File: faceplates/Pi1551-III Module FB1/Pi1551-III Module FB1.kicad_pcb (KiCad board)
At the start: 2 copper layers, 100 x 100 mm, 8 parts, among them M1 Mounting, M2 Mounting, M3 Mounting, M4 Mounting

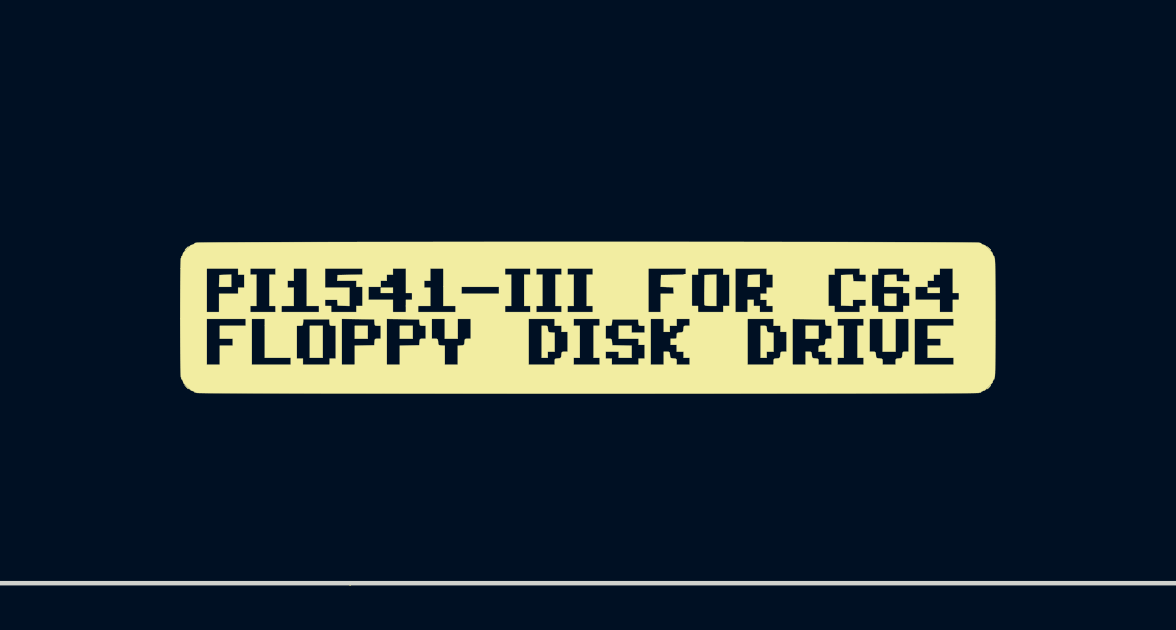
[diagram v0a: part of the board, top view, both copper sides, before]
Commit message: PI1551 branding and Microgramma font labels
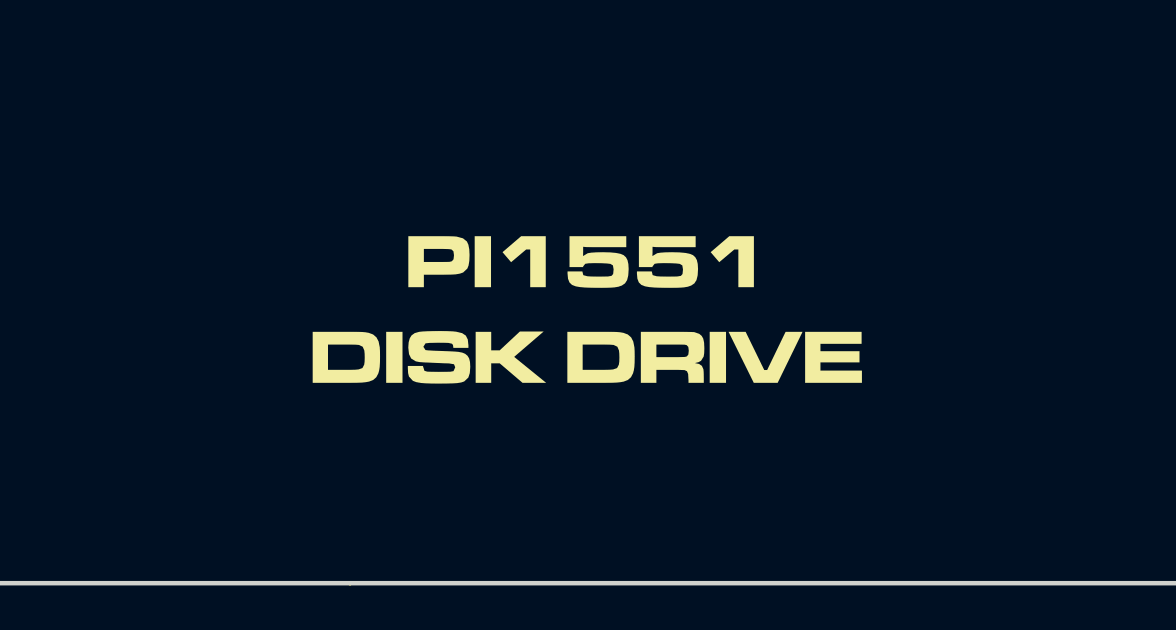
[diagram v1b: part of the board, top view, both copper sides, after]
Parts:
- removed G***: LOGO, Pi1541:Pi1541-Decal2
- removed Pi1541-logo3: , Pi1541:Pi1541-logo3
- added kibuzzard-69864CDD: G***, kibuzzard-69864CDD, B.Cu at (120.2, 91.0)
- added kibuzzard-69864D02: G***, kibuzzard-69864D02, B.Cu at (120.2, 83.0)
- added kibuzzard-69864E12: G***, kibuzzard-69864E12, F.Cu at (120.2, 145.5)

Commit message: gerber files for fabrication
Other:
- board text added: "JLCJLCJLCJLC"
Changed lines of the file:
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@@
 			(disableapertmacros no)
 			(usegerberextensions yes)
-			(usegerberattributes no)
-			(usegerberadvancedattributes no)
+			(usegerberattributes yes)
+			(usegerberadvancedattributes yes)
 			(creategerberjobfile no)
 			(dashed_line_dash_ratio 12.000000)
@@
 			(drillshape 0)
 			(scaleselection 1)
-			(outputdirectory "export/")
+			(outputdirectory "gerbers/")
 		)
 	)
@@
 		(layer "Edge.Cuts")
 	)
+	(gr_text "JLCJLCJLCJLC"
+		(at 167.259 69.596 90)
+		(layer "F.SilkS")
+		(effects
+			(font
+				(size 0.8 0.8)
+				(thickness 0.15)
+			)
+			(justify left bottom)
+		)
+	)
 	(gr_text "5V DC"
